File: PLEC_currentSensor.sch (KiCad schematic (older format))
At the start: 6 parts, among them U6 HXS20

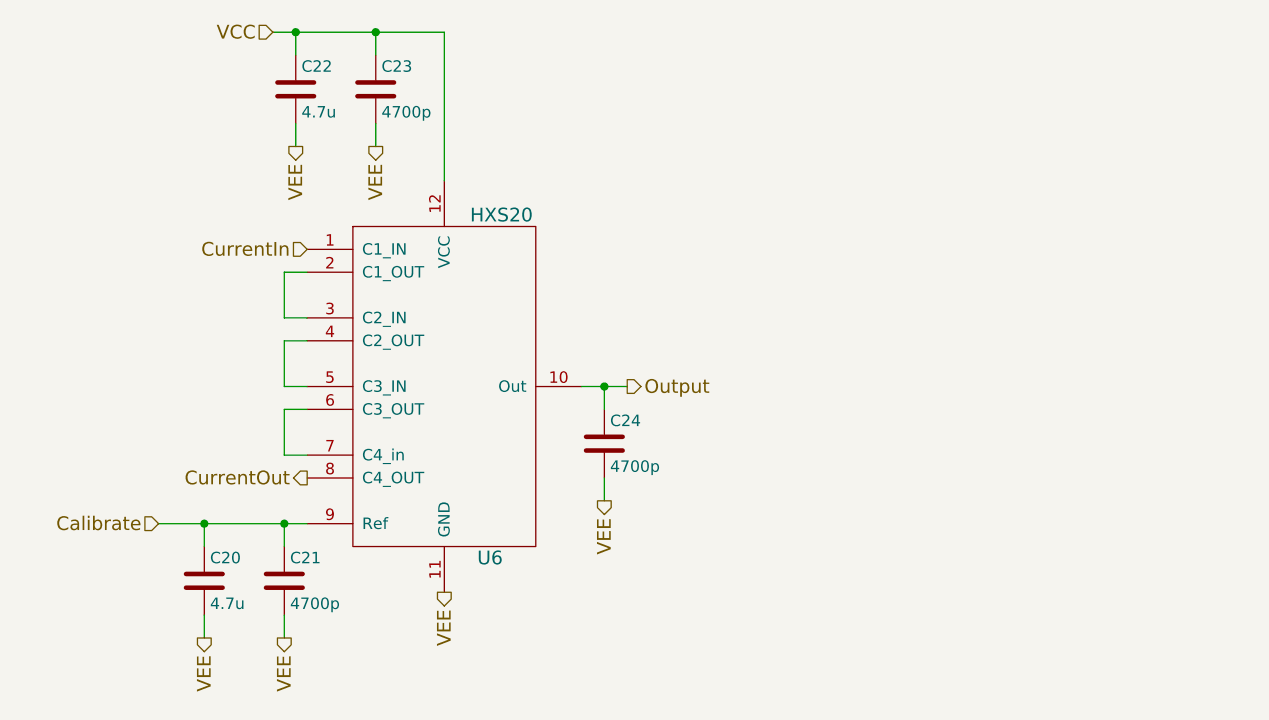
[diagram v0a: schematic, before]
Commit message: Almost done with layout; need to rearrange uC pins
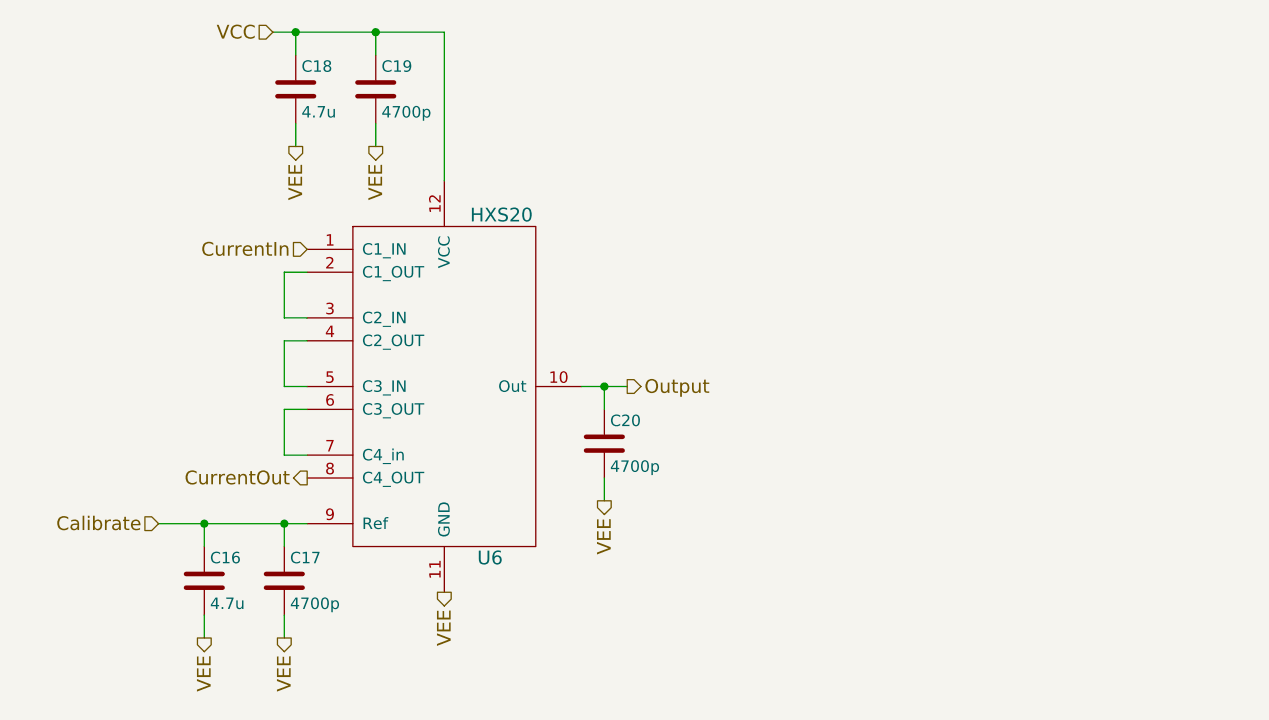
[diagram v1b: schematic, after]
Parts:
- renumbered C20 to C16, C21 to C17, C22 to C18, C23 to C19, C24 to C20
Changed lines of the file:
@@
 Calibrate
 $Comp
-L C C24
+L C C20
 U 1 1 5A76F4F4
 P 6100 4550
-F 0 "C24" H 6125 4650 50  0000 L CNN
+F 0 "C20" H 6125 4650 50  0000 L CNN
 F 1 "4700p" H 6125 4450 50  0000 L CNN
 F 2 "PLEC:THTt_100Px150Lx100Wx183H_4700p" H 6138 4400 50  0001 C CNN
@@
 VEE
 $Comp
-L C C21
+L C C17
 U 1 1 5A76F646
 P 4700 5150
-F 0 "C21" H 4725 5250 50  0000 L CNN
+F 0 "C17" H 4725 5250 50  0000 L CNN
 F 1 "4700p" H 4725 5050 50  0000 L CNN
 F 2 "PLEC:THTt_100Px150Lx100Wx183H_4700p" H 4738 5000 50  0001 C CNN
@@
 Connection ~ 4700 4900
 $Comp
-L C C23
+L C C19
 U 1 1 5A76F788
 P 5100 3000
-F 0 "C23" H 5125 3100 50  0000 L CNN
+F 0 "C19" H 5125 3100 50  0000 L CNN
 F 1 "4700p" H 5125 2900 50  0000 L CNN
 F 2 "PLEC:THTt_100Px150Lx100Wx183H_4700p" H 5138 2850 50  0001 C CNN
@@
 	4650 2750 5400 2750
 $Comp
-L C C22
+L C C18
 U 1 1 5A76F8A4
 P 4750 3000
-F 0 "C22" H 4775 3100 50  0000 L CNN
+F 0 "C18" H 4775 3100 50  0000 L CNN
 F 1 "4.7u" H 4775 2900 50  0000 L CNN
 F 2 "PLEC:THTm_1.5Px4Dx7H_4.7u" H 4788 2850 50  0001 C CNN
@@
 Connection ~ 5100 2750
 $Comp
-L C C20
+L C C16
 U 1 1 5A75C852
 P 4350 5150
-F 0 "C20" H 4375 5250 50  0000 L CNN
+F 0 "C16" H 4375 5250 50  0000 L CNN
 F 1 "4.7u" H 4375 5050 50  0000 L CNN
 F 2 "PLEC:THTm_1.5Px4Dx7H_4.7u" H 4388 5000 50  0001 C CNN

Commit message: Finished PCB with no errors
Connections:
- net COIL1: now reaches U6.2 (C1_OUT), U6.3 (C2_IN)
- net COIL2: now reaches U6.4 (C2_OUT), U6.5 (C3_IN)
- net COIL3: now reaches U6.6 (C3_OUT), U6.7 (C4_in)
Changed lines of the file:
@@
 	4350 5000 4350 4900
 Connection ~ 4350 4900
+Text Label 4700 3950 2    60   ~ 0
+COIL1
+Text Label 4700 4250 2    60   ~ 0
+COIL2
+Text Label 4700 4550 2    60   ~ 0
+COIL3
 $EndSCHEMATC

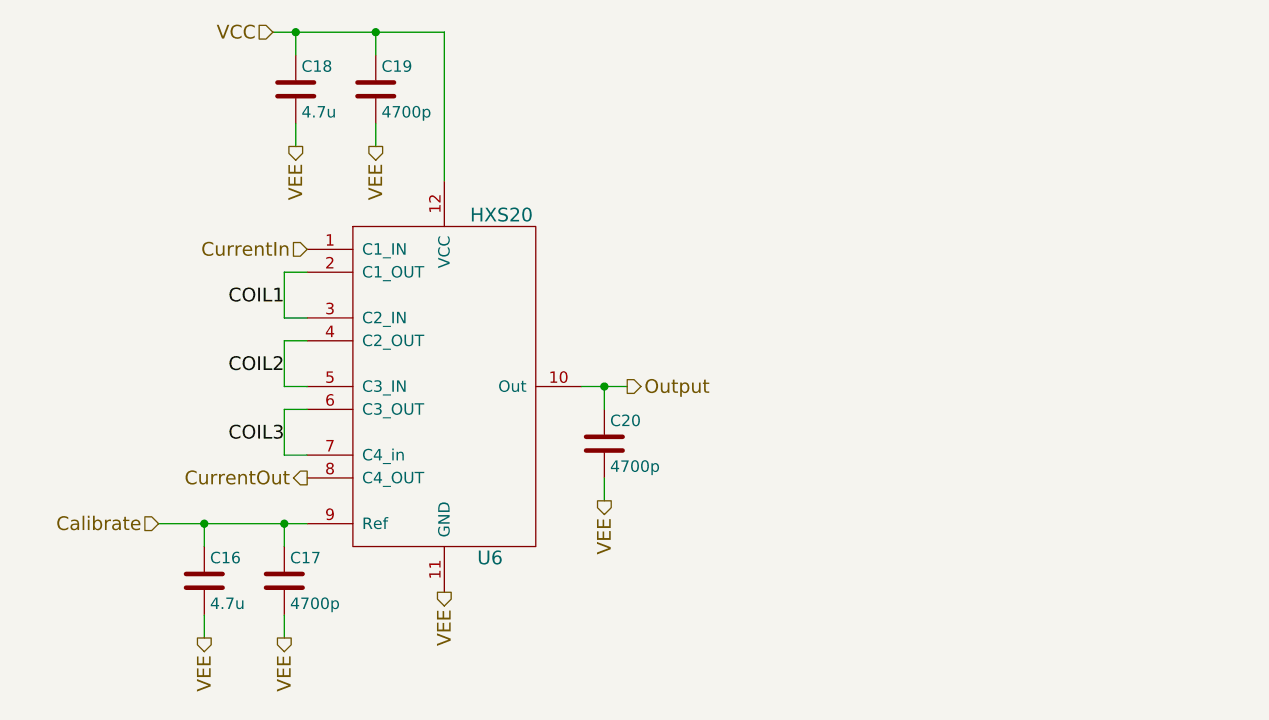
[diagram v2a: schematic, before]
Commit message: Replaced solid state relays with NPN Darlingtons
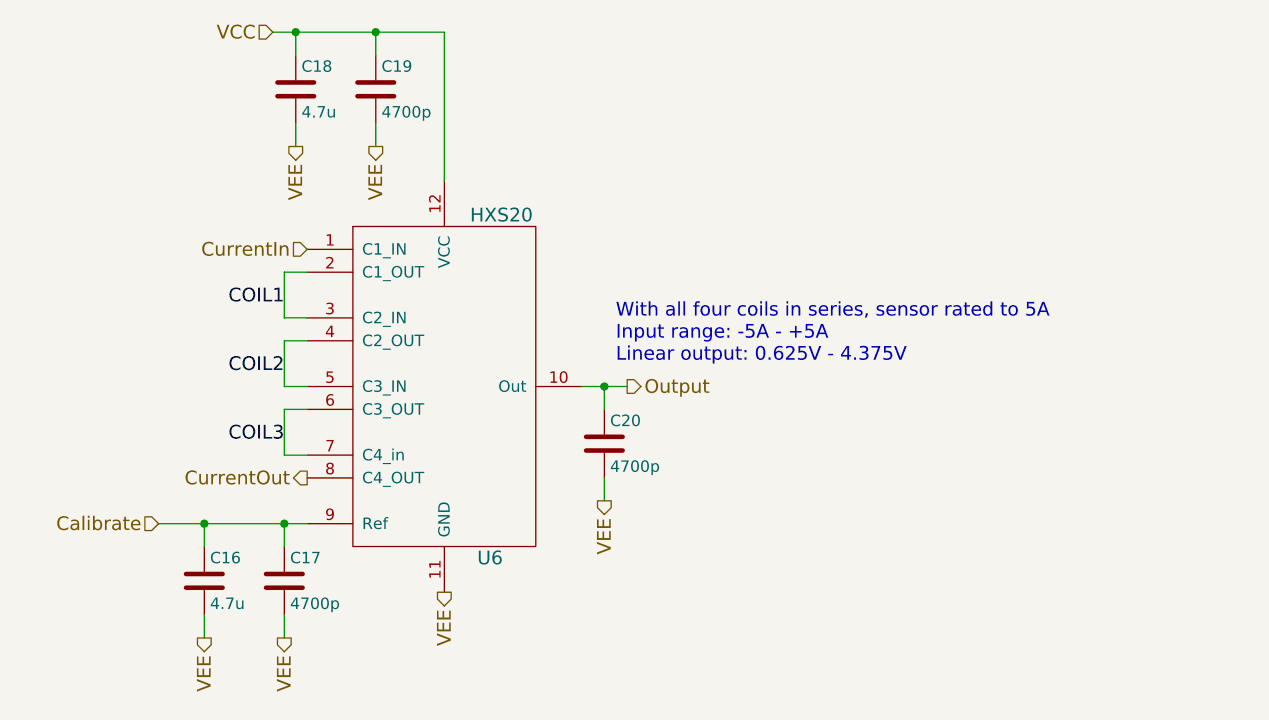
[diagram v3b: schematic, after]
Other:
- note added: "With all four coils in series, sensor rated to 5A\nInput range: -5A - +5A\nLinear output: 0.625V - 4.375V"
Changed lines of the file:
@@
 EESchema Schematic File Version 2
+LIBS:PLEC-rescue
 LIBS:power
 LIBS:device
@@
 LIBS:PLEC
 LIBS:cap_470u
+LIBS:BDW42G
 LIBS:PLEC-cache
 EELAYER 25 0
@@
 $Descr A4 11693 8268
 encoding utf-8
-Sheet 5 9
+Sheet 4 9
 Title ""
 Date ""
@@
 Text Label 4700 4550 2    60   ~ 0
 COIL3
+Text Notes 6150 4200 0    60   ~ 0
+With all four coils in series, sensor rated to 5A\nInput range: -5A - +5A\nLinear output: 0.625V - 4.375V
 $EndSCHEMATC
